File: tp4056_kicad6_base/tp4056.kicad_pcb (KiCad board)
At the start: 2 copper layers, 29 x 23 mm, 31 parts, among them J1 USB_B_Micro, J2 Conn_01x01_Female, J3 Conn_01x01_Female, J4 Conn_01x01_Female, J5 Conn_01x01_Female, J6 Conn_01x01_Female, J7 Conn_01x01_Female, J8 Conn_01x04_Male, Q1 FDN340P, Q2 FS8205A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

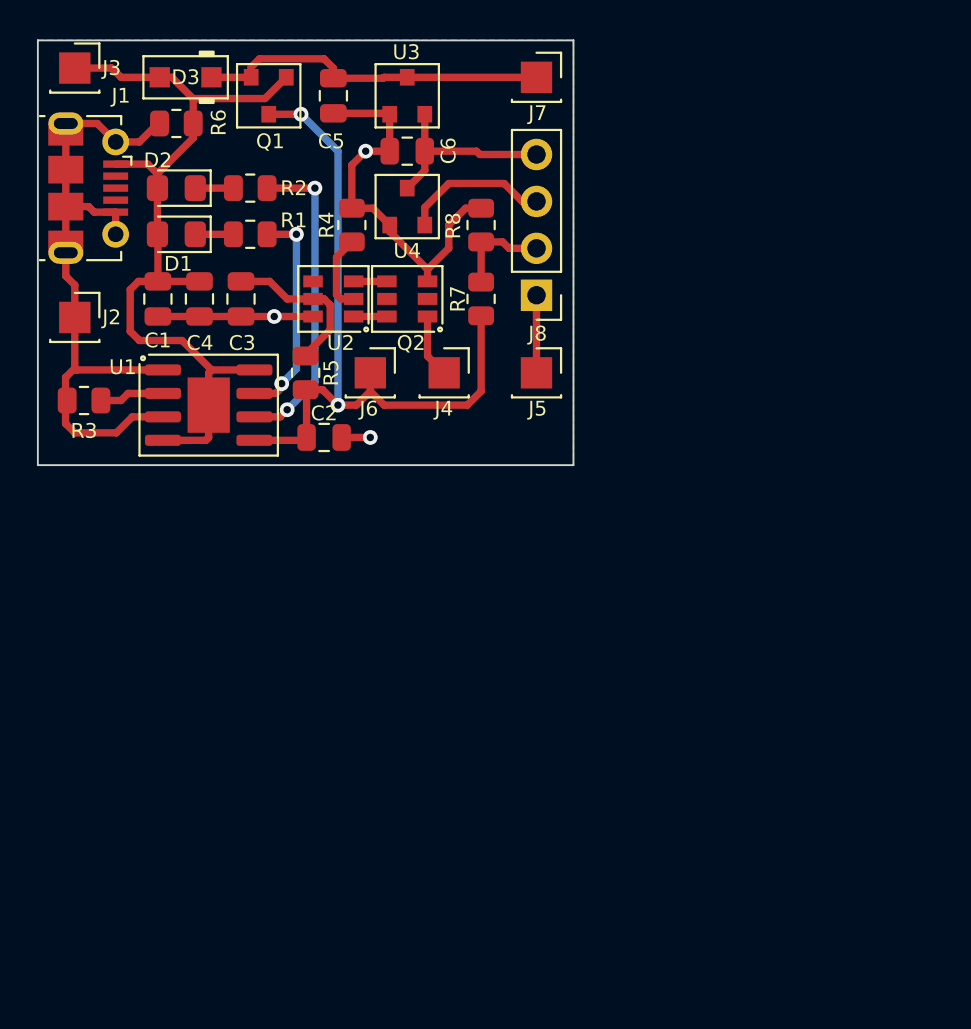
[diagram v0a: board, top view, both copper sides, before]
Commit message: Change conectors. Add jumpers. PCB ready 48x20.
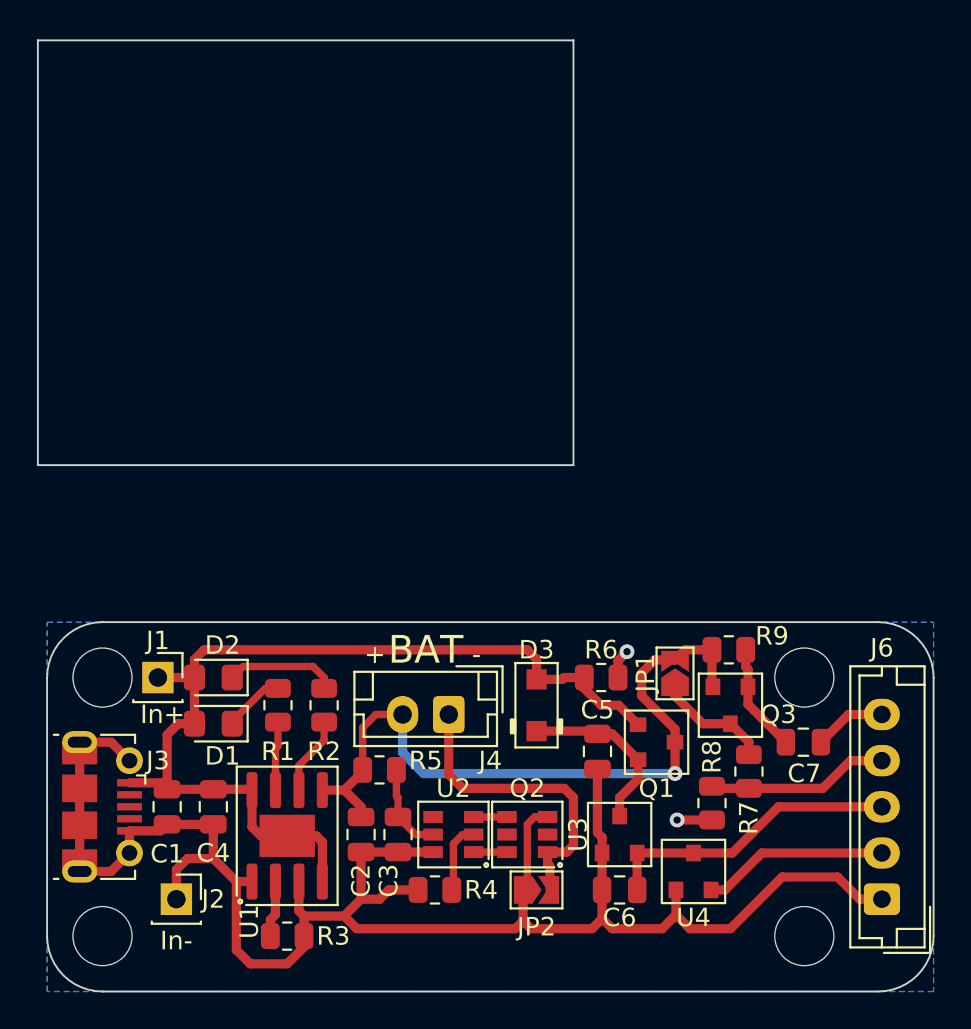
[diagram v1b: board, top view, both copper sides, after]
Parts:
- removed the J3 at (122.0, 57.5)
- removed J5, J7: Conn_01x01_Female, Connector_PinSocket_2.54mm:PinSocket_1x01_P2.54mm_Vertical
- removed J8: Conn_01x04_Male, Connector_PinHeader_2.54mm:PinHeader_1x04_P2.54mm_Vertical
- added ?: , , F.Cu at (161.5, 104.5)
- added ?: , , F.Cu at (161.5, 90.5)
- added ?: , , F.Cu at (123.5, 90.5)
- added C7: 0.1uF, Capacitor_SMD:C_0805_2012Metric, F.Cu at (161.4, 94.0)
- added J1: Conn_01x01_Female, Connector_PinSocket_2.54mm:PinSocket_1x01_P2.54mm_Vertical, F.Cu at (126.5, 90.5)
- added JP1: SolderJumper_2_Open, Jumper:SolderJumper-2_P1.3mm_Open_TrianglePad1.0x1.5mm, F.Cu at (154.5, 90.3)
- added JP2: SolderJumper_2_Open, Jumper:SolderJumper-2_P1.3mm_Open_TrianglePad1.0x1.5mm, F.Cu at (147.0, 102.0)
- added Q3: AO3401A, Package_TO_SOT_SMD_AKL:SOT-23, F.Cu at (157.5, 92.0)
- added R9: 10k, Resistor_SMD:R_0805_2012Metric, F.Cu at (157.4, 89.0)
- added REF**: MountingHole_3.2mm_M3_ISO7380, MountingHole:MountingHole_3.2mm_M3_ISO7380, F.Cu at (123.5, 104.5)
- J4: value Conn_01x01_Female -> Conn_01x02_Male; footprint Connector_PinSocket_2.54mm:PinSocket_1x01_P2.54mm_Vertical -> Connector_JST:JST_EH_B2B-EH-A_1x02_P2.50mm_Vertical
- J6: value Conn_01x01_Female -> Conn_01x05_Male; footprint Connector_PinSocket_2.54mm:PinSocket_1x01_P2.54mm_Vertical -> Connector_JST:JST_EH_B5B-EH-A_1x05_P2.50mm_Vertical
- Q1: value FDN340P -> AO3401A
- R7, R8: value 100k -> 10k
- moved C6 41.6 mm to (151.5, 102.0)
- moved U3 41.6 mm to (151.5, 99.0)
- moved Q1 40.8 mm to (153.5, 94.0), turned to 0 degrees
- moved J6 39.7 mm to (165.7, 102.5), turned to 90 degrees
- moved U4 39.2 mm to (155.5, 101.0)
- moved D3 38.9 mm to (147.0, 92.0), turned to 90 degrees
- moved C5 38.3 mm to (150.3, 94.5)
- moved R6 37.8 mm to (150.5, 90.5), turned to 0 degrees
- moved R4 36.3 mm to (141.5, 102.0), turned to 0 degrees
- moved R8 33.7 mm to (156.5, 97.3), turned to -90 degrees
- moved J3 33.5 mm to (123.5, 97.5)
- moved J2 32.0 mm to (127.5, 102.5)
- moved R3 31.0 mm to (133.5, 104.5), turned to 0 degrees
- moved C3 30.2 mm to (139.5, 99.0)
- moved Q2 29.7 mm to (146.5, 99.0)
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- renumbered J1 to J3
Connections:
- net /BAT- renamed -BATT
- net /OUT+ renamed VDC
- C2 pad 1: /BAT+ -> +BATT
- J6 pad 1: /BAT+ -> Earth
- Q1 pad 3: /BAT+ -> +BATT
- R5 pad 1: /BAT+ -> +BATT
- R7 pad 1: /BAT+ -> Net-(R7-Pad1)
- U1 pad 5: /BAT+ -> +BATT
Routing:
- net /BAT+: track 39.7 -> 0.00 mm, vias 2 -> 0
- net +BATT: track 0.00 -> 39.3 mm, vias 0 -> 1
- net Earth: track 71.1 -> 104.5 mm, vias 3 -> 2
- net -BATT: track 3.42 -> 16.8 mm
- net Net-(R2-Pad2): track 17.1 -> 4.25 mm, vias 2 -> 0
- net VDC: track 19.1 -> 9.61 mm
- net Net-(R1-Pad2): track 12.0 -> 3.74 mm, vias 2 -> 0
- net VBUS: track 45.8 -> 52.2 mm
- net Net-(R7-Pad1): track 0.00 -> 6.21 mm
- net Net-(C7-Pad1): track 0.00 -> 5.90 mm
- net +3.3V: track 10.5 -> 16.3 mm
- net Net-(D2-Pad1): track 1.97 -> 6.06 mm
- net /measurment: track 5.32 -> 9.32 mm
- net /ena_meas: track 0.00 -> 3.92 mm
- net Net-(C3-Pad1): track 8.58 -> 4.88 mm
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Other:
- board size 29 x 23 mm -> 48.5 x 51.5 mm
- board text added: "+"
- board text added: "-"
- board text added: "BAT"
- board text added: "In+"
- board text added: "In-"
